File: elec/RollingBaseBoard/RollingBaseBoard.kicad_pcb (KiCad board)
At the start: 2 copper layers, 80 x 80 mm, 102 parts, among them P1 GP2, P10 UART_2, P11 I2C, P12 Motor, P13 Motor, P14 Encoder2, P15 Motor, P16 Switch, P17 Switch, P18 Switch, P19 Switch, P2 GP2, P20 Switch, P3 GP2, P4 GP2, P5 Bat5V, P6 Bat15V, P7 Encoder, P8 Encoder, P9 UART_1, U1 LMD18201, U2 LMD18201, U3 Teensy3.1

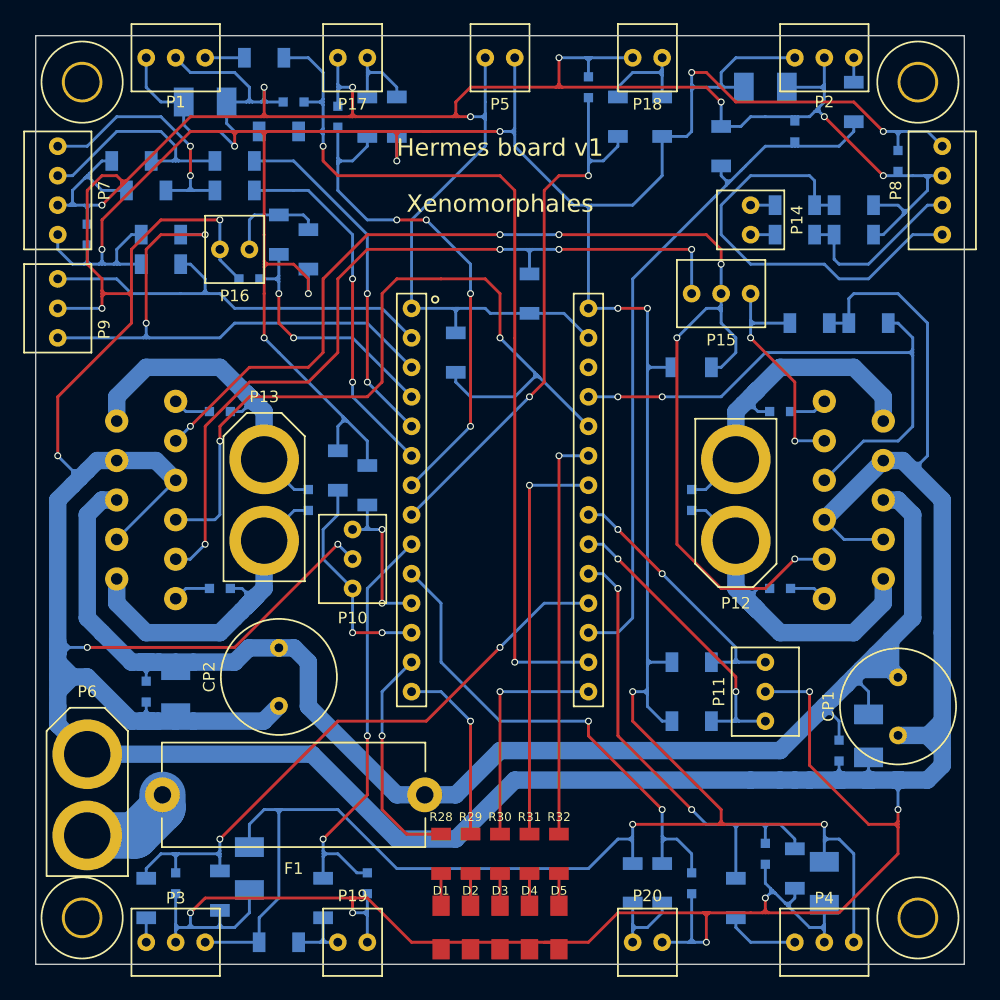
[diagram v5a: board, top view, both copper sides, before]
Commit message: Fixing Hermes footprints and routing, bumped to v2.
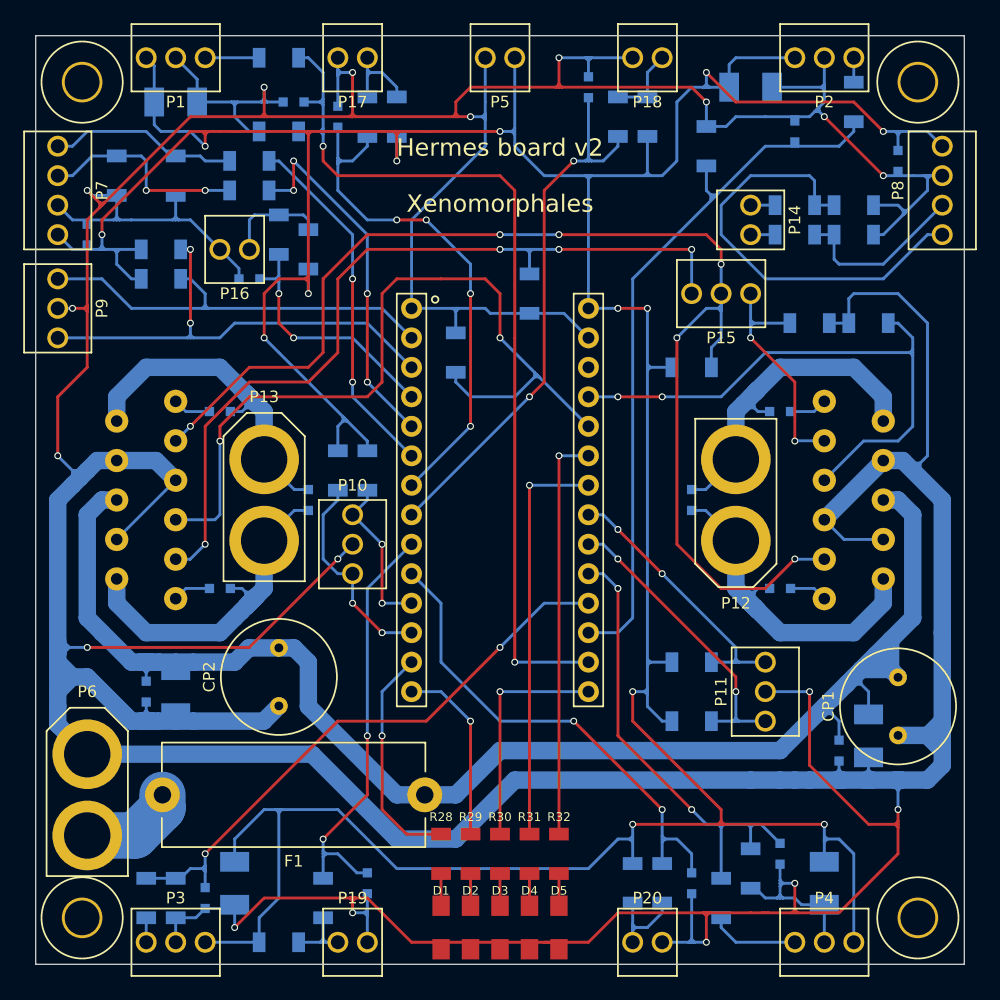
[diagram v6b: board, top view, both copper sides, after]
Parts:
- moved R7 3.86 mm to (120.6, 139.3)
- moved R9 3.81 mm to (170.1, 136.8)
- moved R12 2.84 mm to (120.6, 77.1), turned to 90 degrees
- moved R10 2.84 mm to (126.9, 75.8)
- moved R11 2.84 mm to (126.9, 78.3)
- moved C6 2.84 mm to (123.1, 139.3)
- moved C1 2.54 mm to (120.6, 70.7)
- moved C5 1.80 mm to (125.6, 138.0)
- moved R13 1.80 mm to (115.5, 77.1), turned to 90 degrees
- moved C3 1.27 mm to (170.1, 69.4)
- moved R21 1.27 mm to (137.1, 102.5)
- moved R37 1.27 mm to (161.2, 72.0)
- moved R5 1.27 mm to (166.3, 74.5)
- moved P10 1.27 mm to (135.8, 108.8)
- moved R18 1.27 mm to (119.3, 83.4)
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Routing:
- net /Com/GND: track 708.7 -> 678.3 mm, vias 19 -> 18
- net /Com/+5V: track 370.2 -> 361.0 mm
- net /Com/TX1: track 48.8 -> 41.8 mm
- net Net-(P7-Pad4): track 22.5 -> 16.4 mm, vias 2 -> 0
- net /Teensy/GP2_3: track 54.2 -> 51.0 mm
- net Net-(P18-Pad2): track 9.27 -> 6.45 mm
- net /Teensy/GP2_4: track 43.8 -> 42.0 mm
- net /Driver_1/ThermalFlag: track 109.6 -> 108.1 mm
- net /Teensy/GP2_2: track 61.2 -> 62.7 mm
- net Net-(P7-Pad3): track 19.7 -> 18.2 mm, vias 0 -> 2
- net /Teensy/GP2_1: track 81.3 -> 80.0 mm
- net Net-(P1-Pad1): track 3.38 -> 4.65 mm
- net Net-(P4-Pad1): track 6.45 -> 7.72 mm
- net /Encoder_1/A: track 30.4 -> 31.7 mm, vias 2 -> 4
- net /Teensy/LimitSwitch4: track 43.8 -> 43.1 mm
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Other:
- board text added: "Hermes board v2 Xenomorphales"
- board text removed: "Hermes board v1 Xenomorphales"

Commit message: Final checks and fixes to Hermes v2
It's now ready for production.
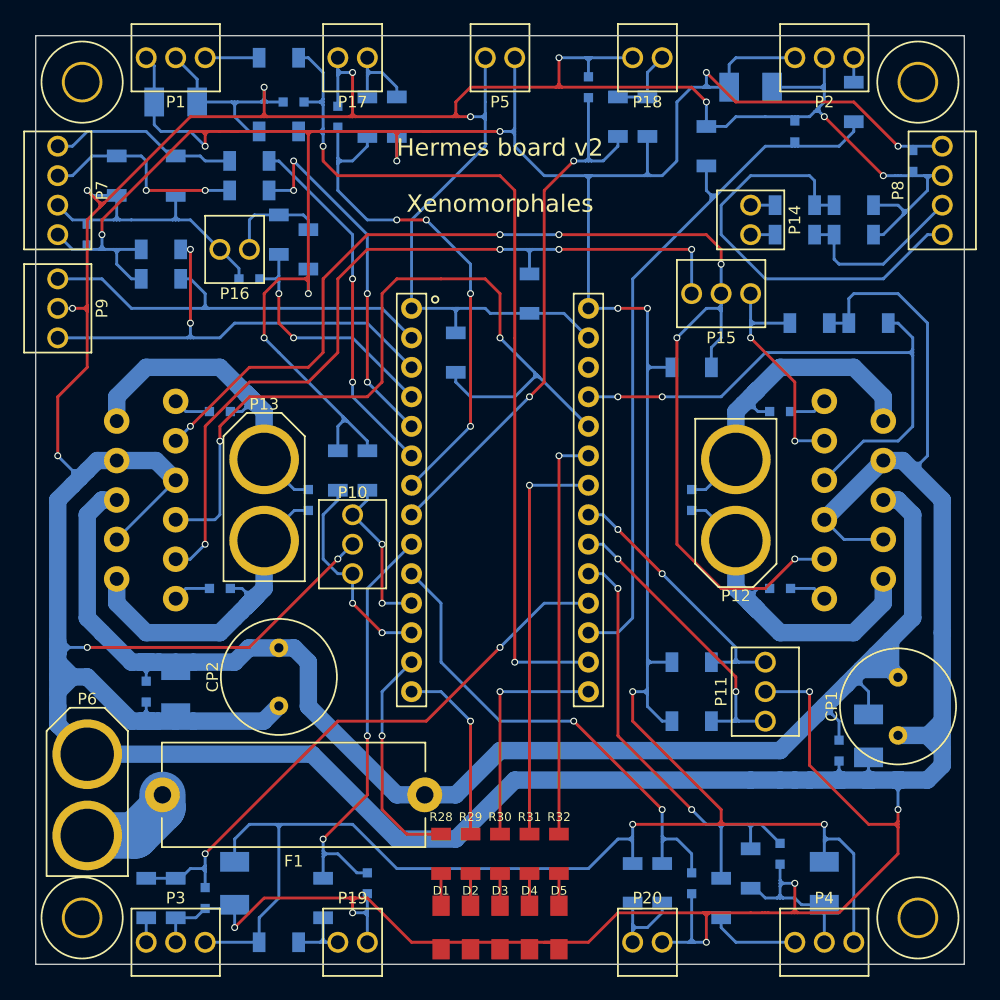
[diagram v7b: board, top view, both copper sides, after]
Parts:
- moved C10 1.27 mm to (184.1, 75.8)
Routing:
- net /Com/+5V: track 361.0 -> 356.1 mm
